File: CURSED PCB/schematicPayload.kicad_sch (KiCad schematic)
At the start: 25 parts, among them J1 Conn_01x02, J2 SD_Card_Device, J3 Conn_PIC_ICSP_ICD, U1 LT1962-3.3, U10 MAX1968xUI, U11 AD9850, U12 LTC6102HVxDD, U13 LTC3886, U14 CY7C65213-28PVXI, U15 ESD224DQA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

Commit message: added stuff
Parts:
- removed TP1: TestPoint, symbol Connector:TestPoint
- removed U10: MAX1968xUI, Package_SO:HTSSOP-28-1EP_4.4x9.7mm_P0.65mm_EP2.85x5.4mm, symbol Driver_TEC:MAX1968xUI
- added D4, D5: LED_Small, symbol Device:LED_Small
- added LD1: PL520, OptoDevice:LaserDiode_TO38ICut-3, symbol Diode_Laser:PL520
- added R1: Heater, symbol Device:Heater
- added R2, R3: R_US, symbol Device:R_US
- added U16: MAX1968xUI, Package_SO:HTSSOP-28-1EP_4.4x9.7mm_P0.65mm_EP2.85x5.4mm, symbol Driver_TEC:MAX1968xUI
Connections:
- net at U8.1 (IN): now also U3.6
- net at U8.2 (OUT): now also U7.5 (IN1)
- net at U8.3 (GND), U8.4 (GND), U8.5 (GND)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: now also U1.3 (BYP), U1.4 (GND), U12.7 (V+), U2.24 (VDD), U3.7 (V+), U7.2 (V_{A}), U9.24 (VB), R3.1, U16.1 (VDD)
- net at RN1.1: now also FB1.2, U5.3 (EN)
- net at RN1.2: now also U6.1 (V+)
- net at RN1.3: now also U5.4 (VIN)
- net at J2.4 (VDD): now also D1.2 (A), U1.5 (~{SHDN}), U1.8 (IN), U13.47 (Iin+), D4.1 (K), R2.1
- net at J2.7 (DAT0): now also U13.4 (Isense0+)
- net at U12.4 (OUT): now also U9.17 (VBL)
- net at D1.1 (K): now also F1.2
- net at U1.1 (OUT): now also FB1.1, U1.2 (SENSE)
- net at U5.5 (VREF): now also U6.5 (V-)
- net at U7.7 (DOUT): now also U2.10 (PA0)
- net at J1.2 (Pin_2): now also U4.1 (GND), U4.2 (GND), U4.3 (GND), U4.7 (GND)
- net at U2.34 (PA13): now also U13.5 (Isense0-)
- net at U2.5 (PH0): now also U9.11 (MCL)
- net at D2.2 (A): now also U3.2 (-), U3.3 (+)
- net at D3.2 (A): now also R1.1
- net at F1.1: now also U4.4 (IN), U4.5 (IN), U4.6 (IN)
- net at U9.8 (MISO/SDA): now also LD1.1 (A)
- new net: D4.2 (A), R2.2
- new net: D5.2 (A), R3.2
- new net: R1.2, U16.10 (LX2), U16.6 (LX2), U16.8 (LX2)
- new net: U16.11 (PVDD2), U16.9 (PVDD2)
- new net: U16.18 (PVDD1), U16.20 (PVDD1)
- new net: U16.19 (LX1), U16.21 (LX1), U16.23 (LX1)
- new net: U16.2 (GND), U16.29 (GND)
- new net: U16.22 (PGND), U16.24 (PGND), U16.5 (PGND), U16.7 (PGND)
- no-connect marks 0 -> 112
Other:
- note added: "Current Amplifier From Fiber"
- note added: "Laser amplifer & output"
- note added: "Power Supply"
- note added: "Voltage noise to ground plate"
- moved on the sheet: D1, D2, D3, F1, FB1, J1, J2, J3, RN1, U1, U11, U12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

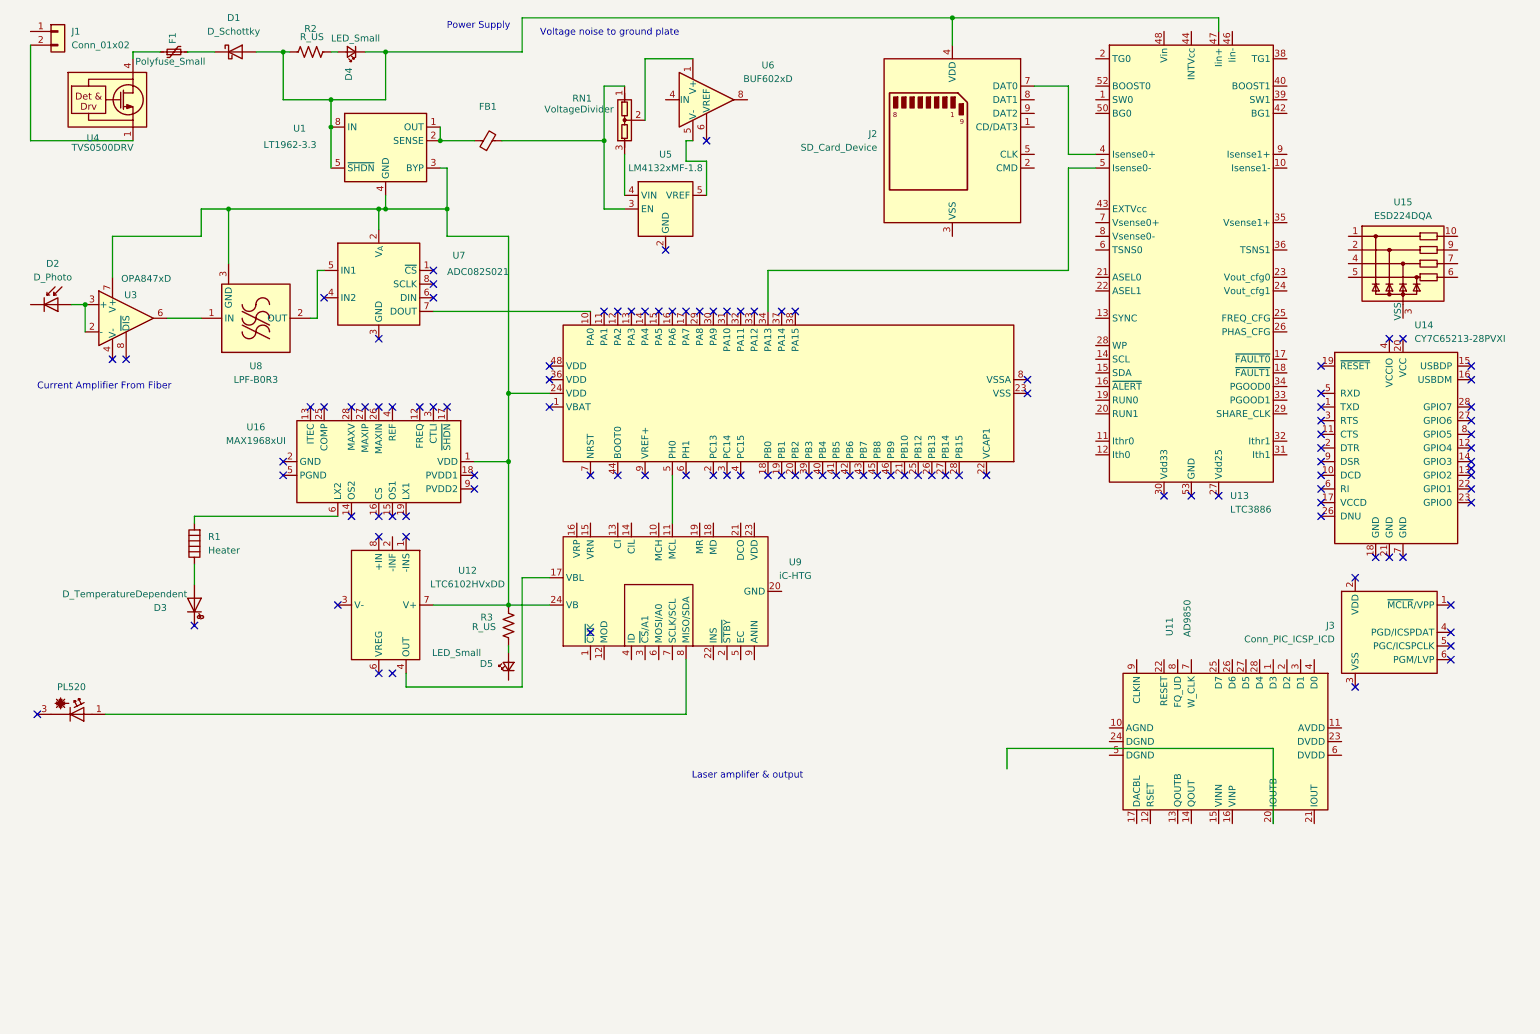
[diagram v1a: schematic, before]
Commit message: Removed Laser output
There was a random laser output deleted it off the schematic to make it cleaner
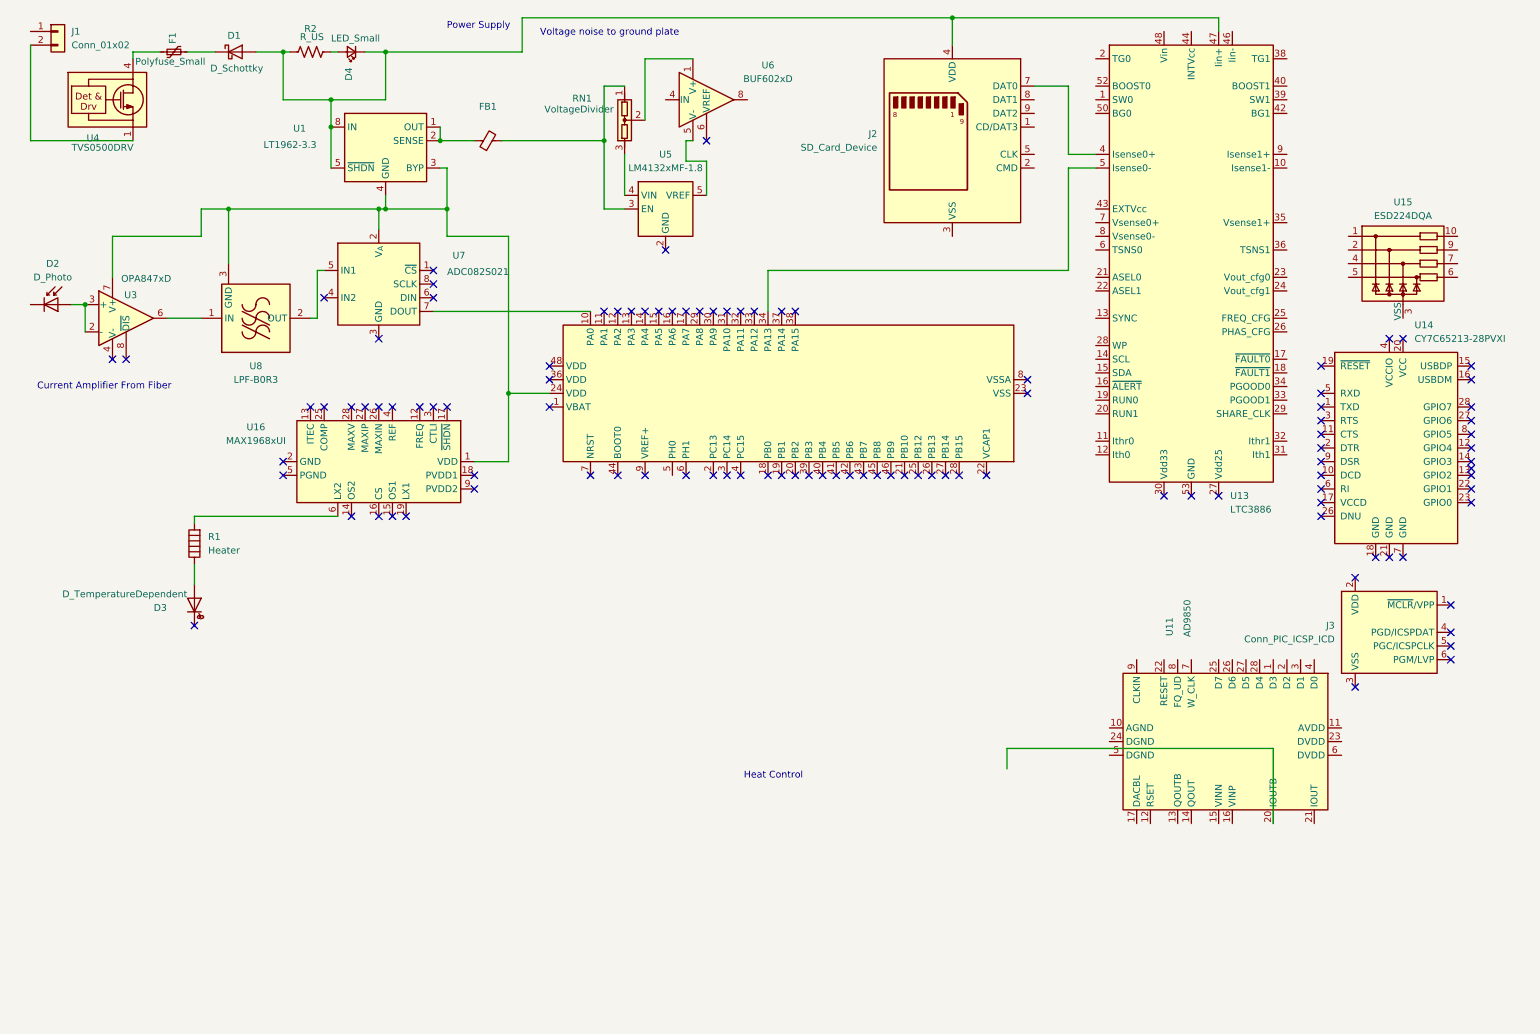
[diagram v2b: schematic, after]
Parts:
- removed D5: LED_Small, symbol Device:LED_Small
- removed LD1: PL520, OptoDevice:LaserDiode_TO38ICut-3, symbol Diode_Laser:PL520
- removed R3: R_US, symbol Device:R_US
- removed U12: LTC6102HVxDD, Package_DFN_QFN:DFN-8-1EP_3x3mm_P0.5mm_EP1.66x2.38mm, symbol Amplifier_Current:LTC6102HVxDD
- removed U9: iC-HTG, Package_DFN_QFN:HVQFN-24-1EP_4x4mm_P0.5mm_EP2.5x2.5mm, symbol Driver_LED:iC-HTG
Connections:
- no-connect marks 112 -> 105
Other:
- note added: "Heat Control"
- note removed: "Laser amplifer & output"
